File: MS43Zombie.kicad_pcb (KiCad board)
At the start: 4 copper layers, 165 x 119.2 mm, 112 parts, among them IC1 NCV8402ASTT1G, IC12 TJA1020T_CM,118, IC14 NCV8402ASTT1G, IC2 M24M02-DRMN6TP, IC27 NCV8402ASTT1G, IC3 NCV8402ASTT1G, IC4 NCV8402ASTT1G, IC5 AD5243BRMZ2.5, IC6 NCV8402ASTT1G, IC7 NCV8402ASTT1G, J1 7-967288-1, J2 EXT1, J3 75867-101LF, J4 EXT2, Q1 MMBT3904, Q2 NCV8461DR2G, Q3 MMBT3904, Q4 MMBT3904, Q5 MMBT3904, Q6 NCV8461DR2G, Q7 MMBT3904, U12 SN65HVD230, U16 SN65HVD230, U19 SN65HVD230, U3 SN65HVD230, U4 SN65HVD230, U8 SN65HVD230

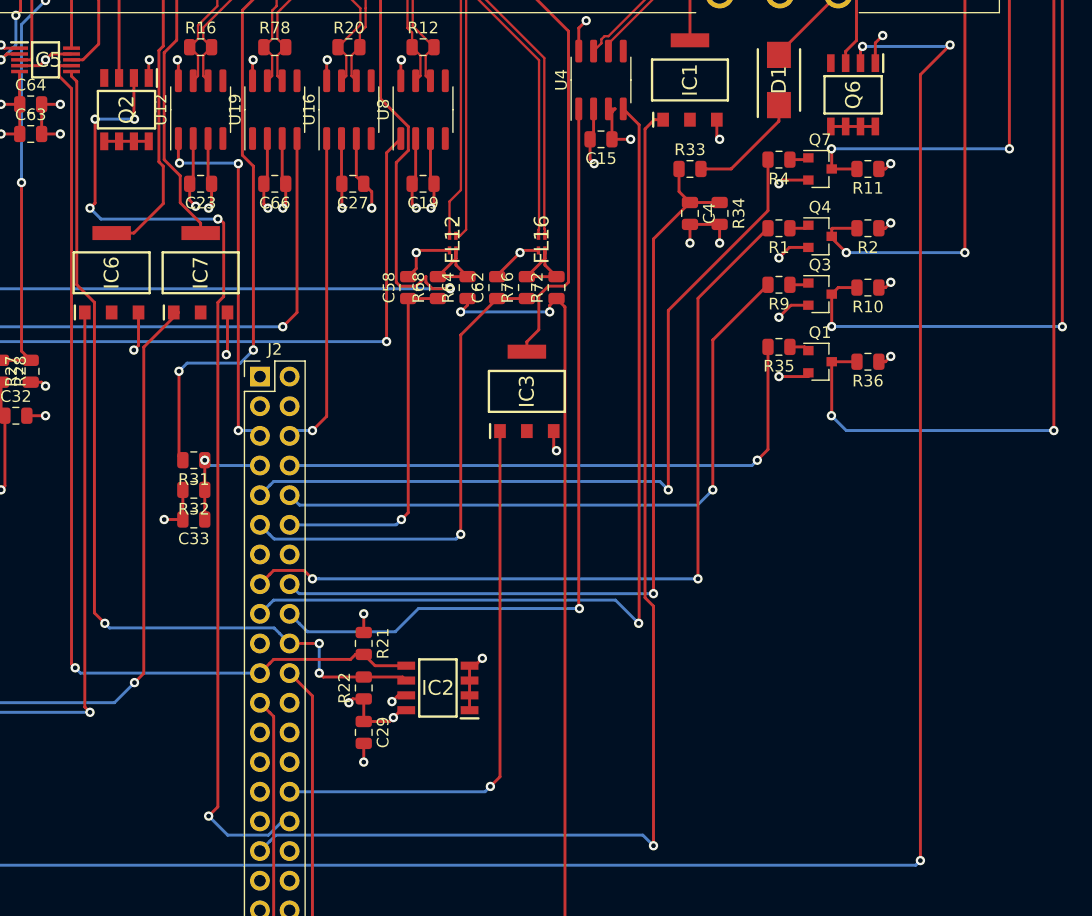
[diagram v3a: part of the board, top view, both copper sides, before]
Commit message: Checkpoint 2022-01-19
Design with bluepill to run the heater since we lose some of the SPI
pins to the USB port on the STM32-H107.
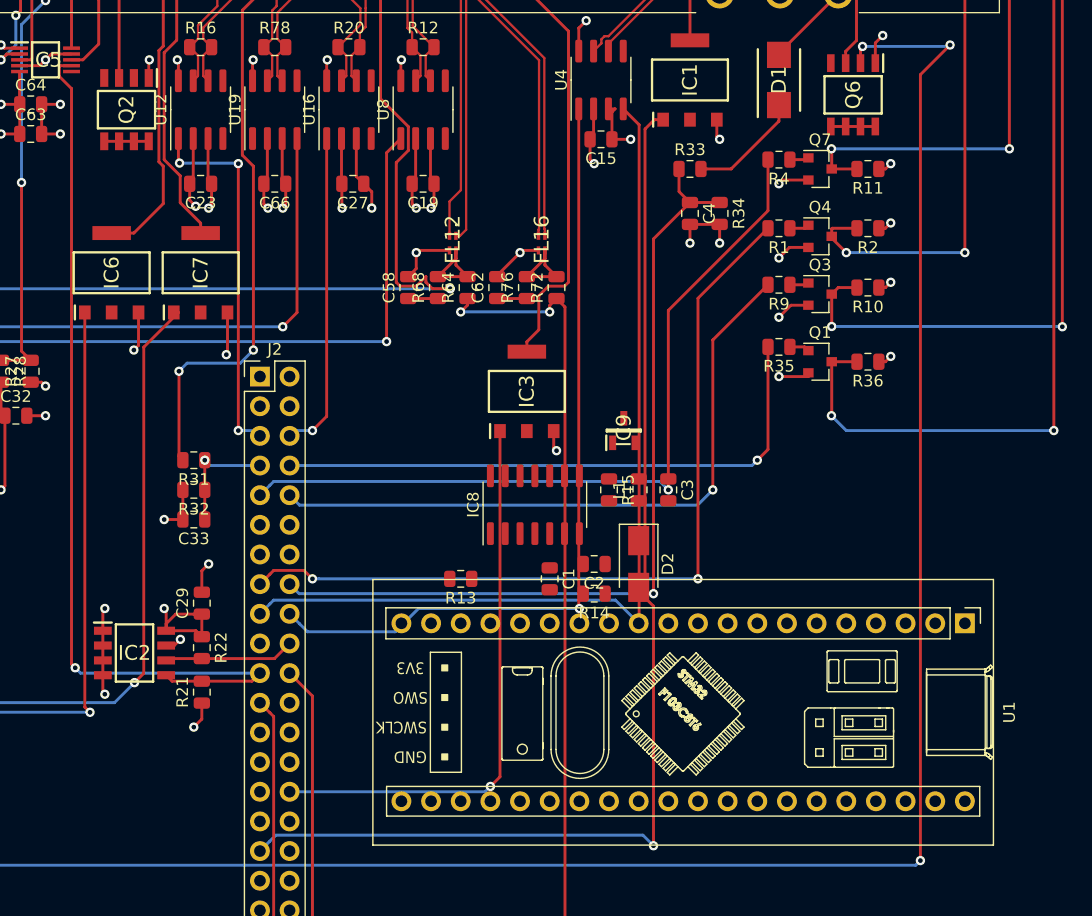
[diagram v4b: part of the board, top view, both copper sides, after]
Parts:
- added C1: 100nF, Capacitor_SMD:C_0805_2012Metric, F.Cu at (185.4, 106.7)
- added C2: 100pF, Capacitor_SMD:C_0805_2012Metric, F.Cu at (189.2, 105.4)
- added C3: 100pF, Capacitor_SMD:C_0805_2012Metric, F.Cu at (195.6, 99.1)
- added D2: MRA4004T3G, Diode_SMD:D_SMA, F.Cu at (193.0, 105.4)
- added IC8: NCV7356D1R2G, Package_SO:SOIC-14_3.9x8.7mm_P1.27mm, F.Cu at (184.2, 100.3)
- added IC9: NUP1105LT1G, SamacSys_Parts:SOT96P237X111-3N, F.Cu at (191.8, 94.0)
- added L1: 47uH, Inductor_SMD:L_0805_2012Metric, F.Cu at (193.0, 99.1)
- added R13: 2K7, Resistor_SMD:R_0805_2012Metric, F.Cu at (177.8, 106.7)
- added R14: 6K49, Resistor_SMD:R_0805_2012Metric, F.Cu at (189.2, 108.0)
- added R15: 1K, Resistor_SMD:R_0805_2012Metric, F.Cu at (190.5, 99.1)
- added U1: YAAJ_BluePill, Footprints:YAAJ_BluePill_1, F.Cu at (221.0, 110.5)
- R51: value R_US -> 1K
- moved IC2 26.2 mm to (149.9, 113.0), turned to 0 degrees
- moved C29 17.7 mm to (155.6, 108.8), turned to 90 degrees
- moved R21 14.5 mm to (155.6, 116.4), turned to 90 degrees
- moved R22 14.3 mm to (155.6, 112.6), turned to 270 degrees
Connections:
- net /SCL renamed /PB8
- net /SDA renamed /PB9
- net /SL1- renamed /PC9
- net /SL2- renamed /PC8
- net /SP renamed /PD12
- net /T15_IN renamed /PD6
- net /UART3_RX renamed /PB11
- net /UART3_TX renamed /PB10
- net /USART2_CLK renamed /PA1
- net /USART2_REQ renamed /PE6
- net /USART2_RX renamed /PA3
- net /USART2_TX renamed /PA2
- C34 pad 1: /REV_IN -> /PA8
- J1 pad C3: Net-(J1-PadC3) -> /IHKA_DEMAND_IN
- J2 pad 11: /MG2_TEMP_IN -> /PE12
- J2 pad 12: /MG1_TEMP_IN -> /PE13
- J4 pad 13: /REV_IN -> /PC12
- J4 pad 18: /PC5 -> /MG1_TEMP_IN
- J4 pad 19: /PC4 -> /MG2_TEMP_IN
- J4 pad 24: Net-(J4-Pad24) -> /PA8
- J4 pad 25: /PA7 -> /LIN_NSLP
- J4 pad 28: /LIN_NSLP -> /PA4
- J4 pad 6: Net-(J4-Pad6) -> /PD2
- J4 pad 7: Net-(J4-Pad7) -> /PD3
- R38 pad 1: /REV_IN -> /PA8
- R39 pad 1: /REV_IN -> /PA8
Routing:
- net /PD12: track 86.1 -> 0.00 mm, vias 5 -> 0
- net /PB8: track 77.8 -> 11.2 mm, vias 3 -> 0
- net /MG2_TEMP_IN: track 41.9 -> 2.54 mm, vias 1 -> 0
- net /MG1_TEMP_IN: track 31.5 -> 2.54 mm, vias 1 -> 0
- net /PB9: track 82.7 -> 77.7 mm
- net /3_3Vcc: track 64.3 -> 68.8 mm
- net GND: track 168.7 -> 172.0 mm
